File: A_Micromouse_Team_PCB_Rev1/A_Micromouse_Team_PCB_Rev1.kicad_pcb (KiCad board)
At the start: 2 copper layers, 13 parts, among them J1 Conn_01x07_Pin, J10 Conn_01x06, J2 Conn_01x07_Pin, J3 Conn_01x07_Pin, J4 Conn_01x07_Pin, J5 Conn_01x06_Pin, J6 Conn_01x06_Pin, J7 Conn_01x04_Socket, J8 Conn_01x07_Pin, J9 Conn_01x02_Socket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

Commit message: checked all footprints and created a max footprint
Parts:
- removed J1, J2, J3, J4, J8: Conn_01x07_Pin, Connector_PinHeader_2.54mm:PinHeader_1x07_P2.54mm_Vertical
- removed J10: Conn_01x06, Connector_PinHeader_2.00mm:PinHeader_1x06_P2.00mm_Vertical
- removed J5, J6: Conn_01x06_Pin, Connector_PinSocket_2.54mm:PinSocket_1x06_P2.54mm_Vertical
- removed J7: Conn_01x04_Socket, Connector_PinHeader_2.00mm:PinHeader_1x04_P2.00mm_Vertical
- removed J9: Conn_01x02_Socket, Connector_PinHeader_2.00mm:PinHeader_1x02_P2.00mm_Vertical
- removed U1: Teensy4.0, Teensy4.0:Teensy40
- removed U2: BNO055, Package_LGA:LGA-28_5.2x3.8mm_P0.5mm
- removed U3: TB6612FNG, Package_SO:SSOP-24_5.3x8.2mm_P0.65mm
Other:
- board outline added: 106.7 x 127 mm

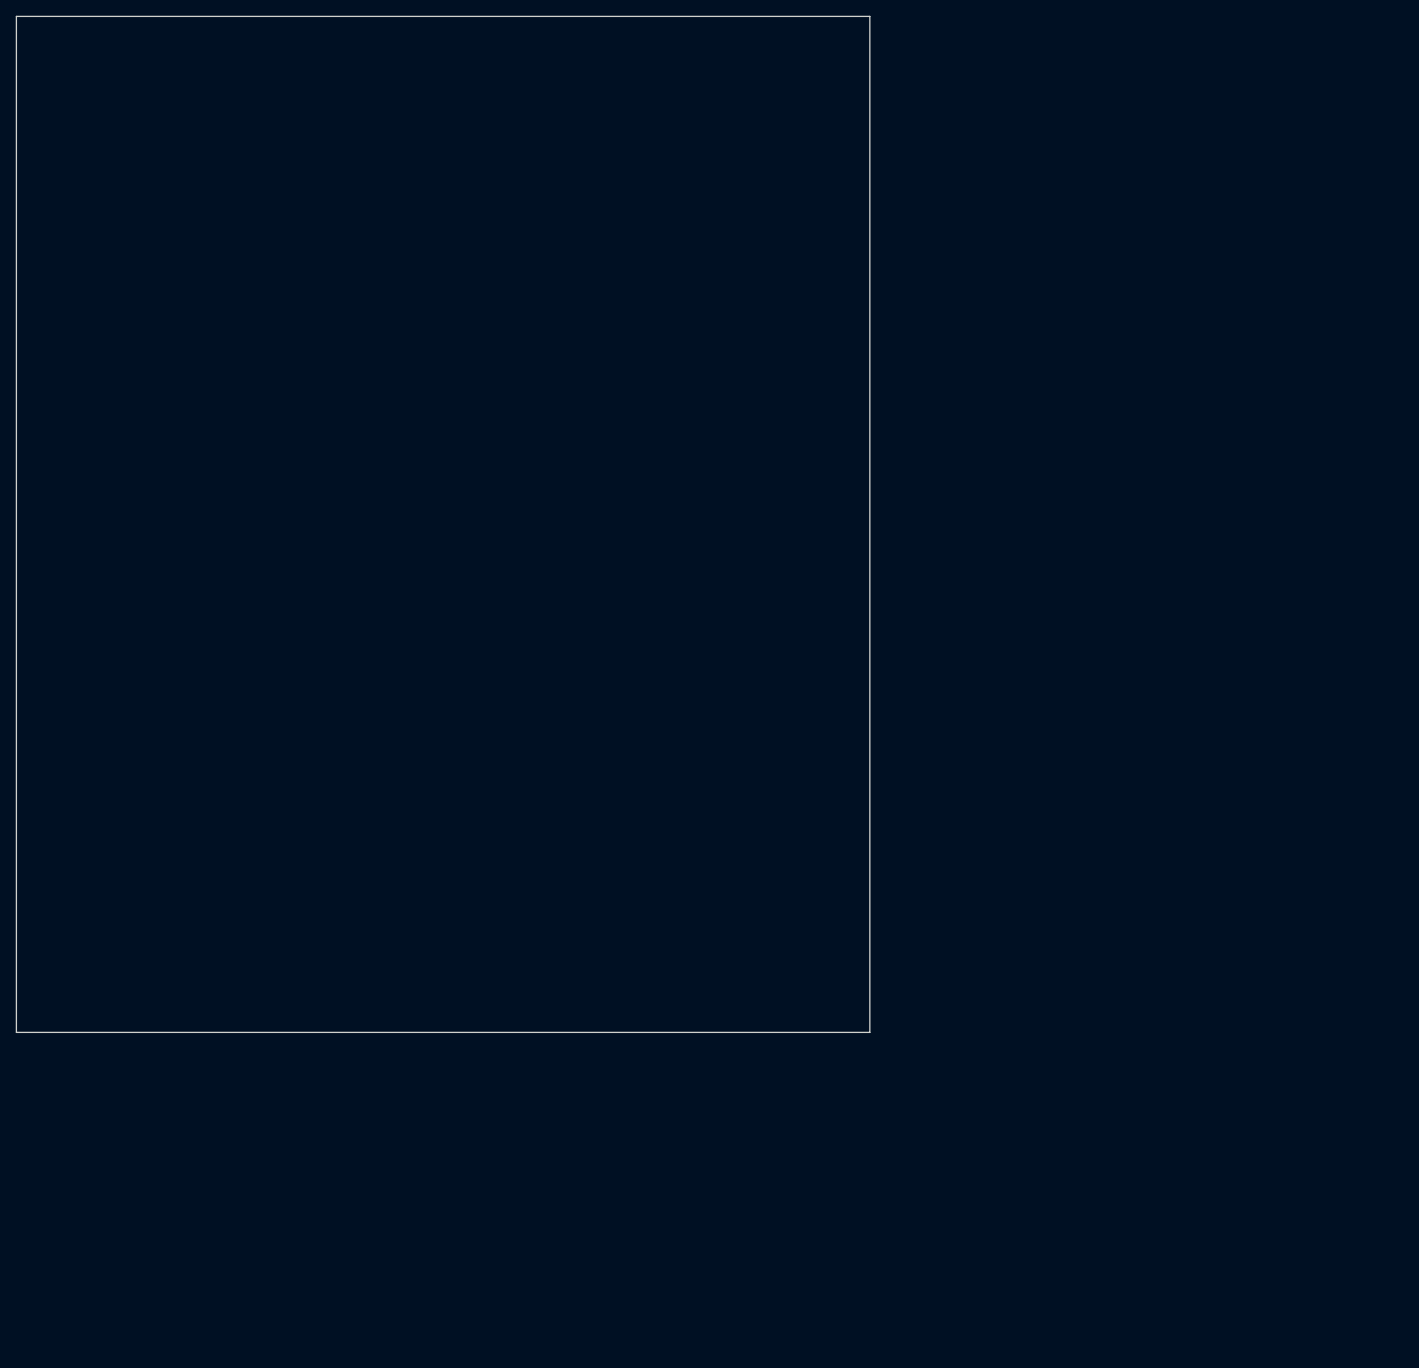
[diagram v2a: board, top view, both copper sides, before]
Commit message: started footprint layout
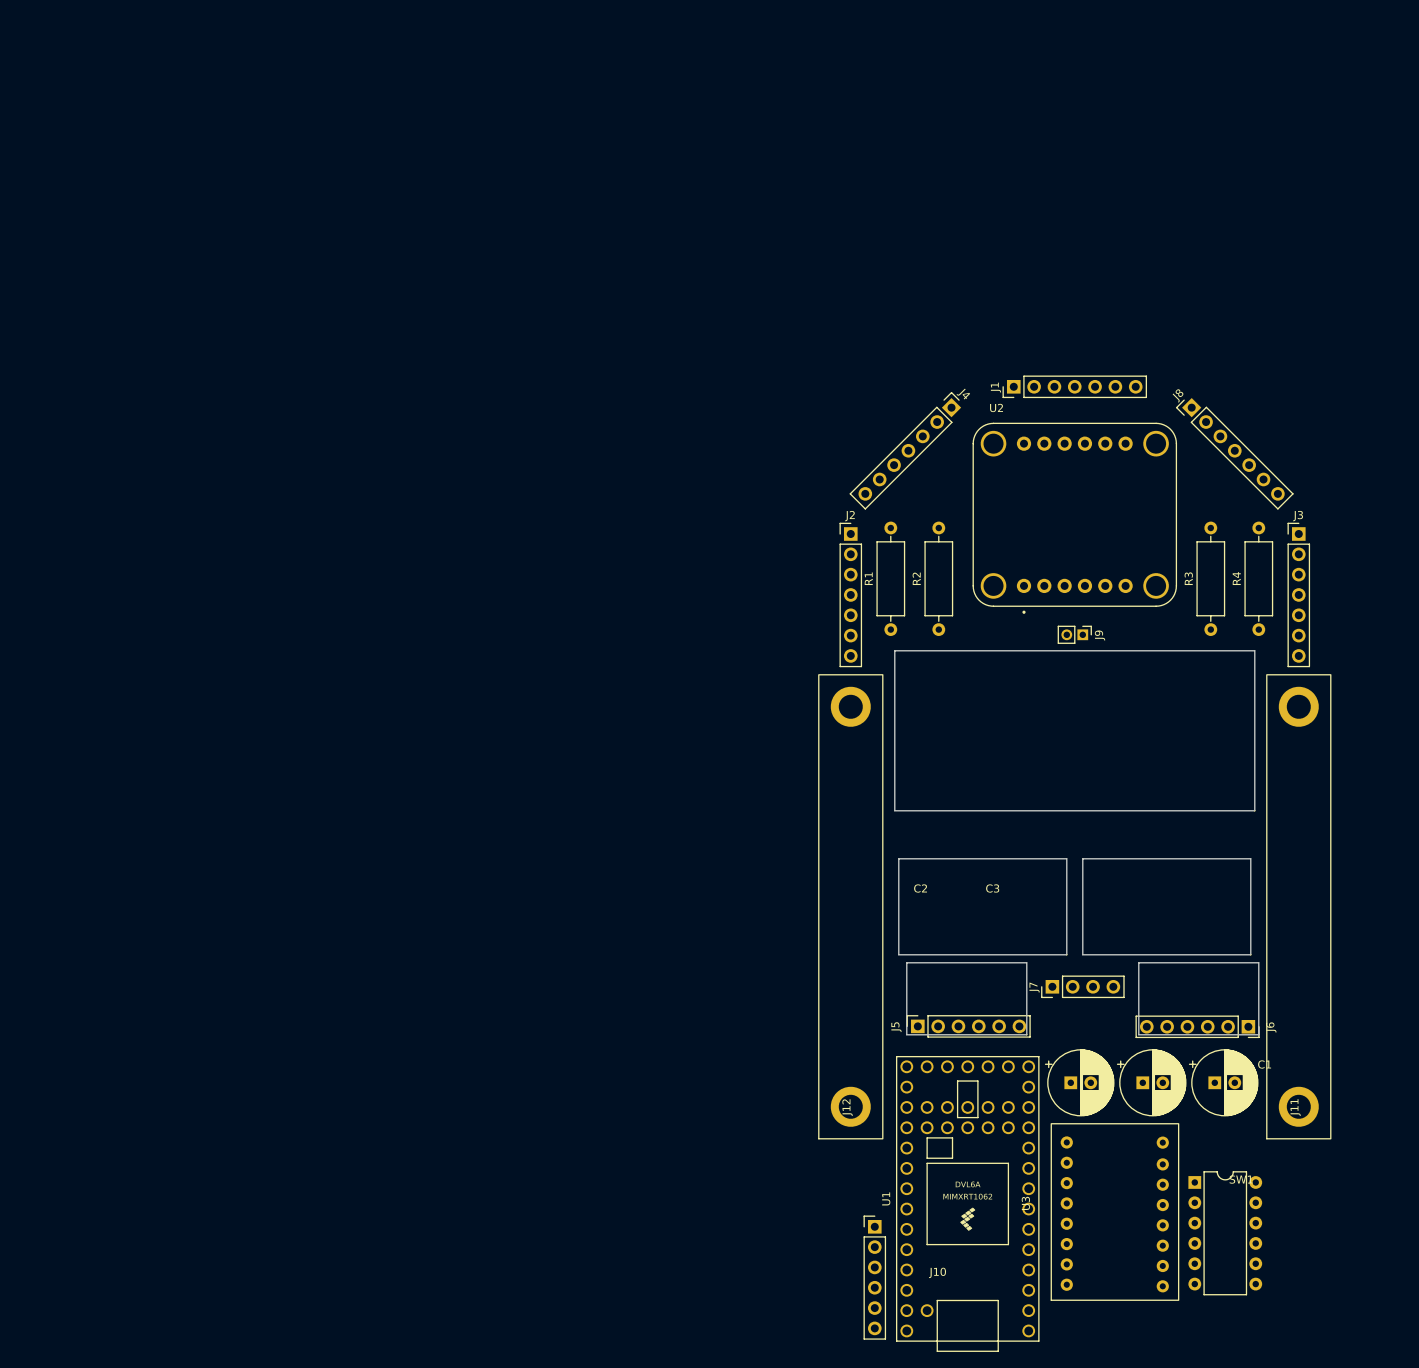
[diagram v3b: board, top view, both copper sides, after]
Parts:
- added C1: C, Capacitor_THT:CP_Radial_D8.0mm_P2.50mm, F.Cu at (162.5, 146.0)
- added C2: C, Capacitor_THT:CP_Radial_D8.0mm_P2.50mm, F.Cu at (144.5, 146.0)
- added C3: C, Capacitor_THT:CP_Radial_D8.0mm_P2.50mm, F.Cu at (153.5, 146.0)
- added J1: TOF2, Connector_PinHeader_2.54mm:PinHeader_1x07_P2.54mm_Vertical, F.Cu at (137.4, 59.0)
- added J10: 5V->12V, Connector_PinHeader_2.54mm:PinHeader_1x06_P2.54mm_Vertical, F.Cu at (120.0, 164.0)
- added J11: MotorCageMount, MicromouseLibaryNew:motorMount, F.Cu at (173.0, 149.0)
- added J12: MotorCageMount, MicromouseLibaryNew:motorMount, F.Cu at (117.0, 149.0)
- added J2: TOF3, Connector_PinHeader_2.54mm:PinHeader_1x07_P2.54mm_Vertical, F.Cu at (117.0, 77.4)
- added J3: TOF4, Connector_PinHeader_2.54mm:PinHeader_1x07_P2.54mm_Vertical, F.Cu at (173.0, 77.4)
- added J4: TOF5, Connector_PinHeader_2.54mm:PinHeader_1x07_P2.54mm_Vertical, F.Cu at (129.6, 61.6)
- added J5: Motor1, Connector_PinSocket_2.54mm:PinSocket_1x06_P2.54mm_Vertical, F.Cu at (125.4, 138.9)
- added J6: Motor2, Connector_PinSocket_2.54mm:PinSocket_1x06_P2.54mm_Vertical, F.Cu at (166.7, 139.0)
- added J7: NeoPixel, Connector_PinHeader_2.54mm:PinHeader_1x04_P2.54mm_Vertical, F.Cu at (142.2, 134.0)
- added J8: TOF1, Connector_PinHeader_2.54mm:PinHeader_1x07_P2.54mm_Vertical, F.Cu at (159.6, 61.6)
- added J9: Battery, Connector_PinHeader_2.00mm:PinHeader_1x02_P2.00mm_Vertical, F.Cu at (146.0, 90.0)
- added R1: R_US, Resistor_THT:R_Axial_DIN0309_L9.0mm_D3.2mm_P12.70mm_Horizontal, F.Cu at (122.0, 89.3)
- added R2: R_US, Resistor_THT:R_Axial_DIN0309_L9.0mm_D3.2mm_P12.70mm_Horizontal, F.Cu at (128.0, 89.3)
- added R3: R_US, Resistor_THT:R_Axial_DIN0309_L9.0mm_D3.2mm_P12.70mm_Horizontal, F.Cu at (162.0, 89.3)
- added R4: R_US, Resistor_THT:R_Axial_DIN0309_L9.0mm_D3.2mm_P12.70mm_Horizontal, F.Cu at (168.0, 89.3)
- added SW1: SW_DIP_x06, Package_DIP:DIP-12_W7.62mm, F.Cu at (160.0, 158.5)
- added U1: Teensy4.0, MicromouseLibaryNew:Teensy40, F.Cu at (131.6, 160.5)
- added U2: IMU, MicromouseLibaryNew:MODULE_4754, F.Cu at (145.0, 75.0)
- added U3: MotorController, MicromouseLibaryNew:MotorController, F.Cu at (144.0, 171.2)
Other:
- board size 106.7 x 127 mm -> 45.5 x 48 mm

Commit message: Add files via upload
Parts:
- removed C1, C2, C3: C, Capacitor_THT:CP_Radial_D8.0mm_P2.50mm
- added J13: Battery, Connector_PinHeader_2.00mm:PinHeader_1x02_P2.00mm_Vertical, F.Cu at (163.0, 91.0)
- added R5: R_US, Resistor_THT:R_Axial_DIN0309_L9.0mm_D3.2mm_P12.70mm_Horizontal, F.Cu at (143.0, 152.3)
- added R6: R_US, Resistor_THT:R_Axial_DIN0309_L9.0mm_D3.2mm_P12.70mm_Horizontal, F.Cu at (139.0, 151.0)
- J2: value TOF3 -> locked
- moved R1 91.1 mm to (164.3, 170.0), turned to 180 degrees
- moved R2 84.8 mm to (164.3, 166.0), turned to 180 degrees
- moved R3 72.7 mm to (164.3, 162.0), turned to 180 degrees
- moved R4 68.7 mm to (164.3, 158.0), turned to 180 degrees
- moved J7 59.0 mm to (141.4, 75.0)
- moved U3 41.6 mm to (161.0, 133.2), turned to -90 degrees
- moved J10 19.4 mm to (123.8, 145.0), turned to 90 degrees
- moved J9 19.0 mm to (127.0, 89.0), turned to 0 degrees
- moved J3 18.1 mm to (183.0, 92.5), turned to 180 degrees
- moved J1 17.8 mm to (152.7, 50.0), turned to -90 degrees
- moved J8 16.9 mm to (175.8, 66.4), turned to -135 degrees
- moved SW1 16.1 mm to (176.1, 157.7)
- moved J2 10.0 mm to (107.0, 77.3)
- moved U1 7.73 mm to (124.3, 163.0), turned to 0 degrees
- moved J4 7.45 mm to (125.2, 55.6)
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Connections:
- J10 pad 4: +5V -> +5VD
- J10 pad 5: unconnected-(J10-Pin_5-Pad5) -> +5VD
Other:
- board size 45.5 x 48 mm -> 82 x 129 mm

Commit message: finished pcb layout (hopefully)
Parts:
- moved J7 15.0 mm to (141.4, 90.0)
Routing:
- net GND: track 0.00 -> 453.3 mm, vias 0 -> 4
- net +5V: track 0.00 -> 400.0 mm, vias 0 -> 13
- net SDA: track 0.00 -> 255.6 mm, vias 0 -> 8
- net SCL: track 0.00 -> 243.0 mm, vias 0 -> 8
- net TOF1: track 0.00 -> 165.1 mm, vias 0 -> 1
- net TOF2: track 0.00 -> 165.0 mm, vias 0 -> 2
- net TOF4: track 0.00 -> 149.1 mm, vias 0 -> 5
- net Net-(J9-Pin_1): track 0.00 -> 117.1 mm, vias 0 -> 1
- net TOF5: track 0.00 -> 111.6 mm, vias 0 -> 2
- net +5VD: track 0.00 -> 100.9 mm, vias 0 -> 2
- net TOF3: track 0.00 -> 96.9 mm, vias 0 -> 3
- net Net-(J7-Pin_2): track 0.00 -> 90.0 mm, vias 0 -> 2
- net +3.3V: track 0.00 -> 86.2 mm, vias 0 -> 5
- net Net-(U1-0_RX1_CRX2_CS1): track 0.00 -> 80.3 mm, vias 0 -> 1
- net Net-(U1-1_TX1_CTX2_MISO1): track 0.00 -> 75.7 mm, vias 0 -> 3
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
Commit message: Add files via upload
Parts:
- moved J7 66.7 mm to (161.0, 153.8), turned to 180 degrees
- moved SW1 62.8 mm to (113.3, 158.5)
- moved J5 47.1 mm to (119.0, 92.3), turned to 180 degrees
- moved J6 42.7 mm to (170.5, 92.3), turned to 180 degrees
- moved R1 40.4 mm to (124.0, 172.3), turned to 90 degrees
- moved R2 36.9 mm to (128.0, 172.3), turned to 90 degrees
- moved R4 35.0 mm to (132.0, 144.7), turned to -90 degrees
- moved R3 34.0 mm to (132.0, 172.3), turned to 90 degrees
- moved J10 33.4 mm to (156.0, 154.0), turned to 180 degrees
- moved U3 25.4 mm to (155.2, 158.0), turned to 0 degrees
- moved J13 22.1 mm to (161.0, 69.0), turned to 45 degrees
- moved U1 21.3 mm to (143.6, 154.1), turned to 90 degrees
- moved J9 18.6 mm to (127.6, 70.4), turned to 135 degrees
- moved R5 16.9 mm to (128.0, 144.7), turned to -90 degrees
- moved R6 16.3 mm to (124.0, 157.3), turned to 90 degrees
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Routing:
- net GND: track 453.3 -> 0.00 mm, vias 4 -> 0
- net +5V: track 400.0 -> 0.00 mm, vias 13 -> 0
- net SDA: track 255.6 -> 0.00 mm, vias 8 -> 0
- net SCL: track 243.0 -> 0.00 mm, vias 8 -> 0
- net TOF1: track 165.1 -> 0.00 mm, vias 1 -> 0
- net TOF2: track 165.0 -> 0.00 mm, vias 2 -> 0
- net TOF4: track 149.1 -> 0.00 mm, vias 5 -> 0
- net Net-(J9-Pin_1): track 117.1 -> 0.00 mm, vias 1 -> 0
- net TOF5: track 111.6 -> 0.00 mm, vias 2 -> 0
- net +5VD: track 100.9 -> 0.00 mm, vias 2 -> 0
- net TOF3: track 96.9 -> 0.00 mm, vias 3 -> 0
- net Net-(J7-Pin_2): track 90.0 -> 0.00 mm, vias 2 -> 0
- net +3.3V: track 86.2 -> 0.00 mm, vias 5 -> 0
- net Net-(U1-0_RX1_CRX2_CS1): track 80.3 -> 0.00 mm, vias 1 -> 0
- net Net-(U1-1_TX1_CTX2_MISO1): track 75.7 -> 0.00 mm, vias 3 -> 0
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
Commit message: Add files via upload
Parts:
- moved J6 12.4 mm to (171.0, 80.0), turned to 0 degrees
- moved J1 4.00 mm to (152.6, 53.0)
- moved J4 3.76 mm to (128.0, 57.2)
- moved J8 3.69 mm to (173.0, 68.0)
- moved J10 1.21 mm to (156.9, 153.2)
- moved J7 1.21 mm to (161.9, 153.0)
- moved R1 1.21 mm to (124.9, 171.5)
- moved R2 1.21 mm to (128.9, 171.5)
- moved R3 1.21 mm to (132.9, 171.5)
- moved R4 1.21 mm to (132.9, 143.8)
- moved R5 1.21 mm to (128.9, 143.8)
- moved R6 1.21 mm to (124.9, 156.5)
- moved SW1 1.21 mm to (114.2, 157.7)
- moved U1 1.21 mm to (144.5, 153.3)
- moved U3 1.21 mm to (156.1, 157.2)
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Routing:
- net GND: track 0.00 -> 340.1 mm, vias 0 -> 11
- net +5V: track 0.00 -> 153.8 mm, vias 0 -> 7
- net SDA: track 0.00 -> 142.7 mm, vias 0 -> 8
- net SCL: track 0.00 -> 138.2 mm, vias 0 -> 7
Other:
- board size 82 x 129 mm -> 66 x 126 mm
